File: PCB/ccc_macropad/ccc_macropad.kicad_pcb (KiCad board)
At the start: 2 copper layers, 101.5 x 44 mm, 18 parts, among them SW1 SW_Push, SW2 SW_Push, SW3 OS/Left_Right-hand_Switch, SW4 SW_Push, SW5 SW_Push, U2 XIAO-RP2040-DIP

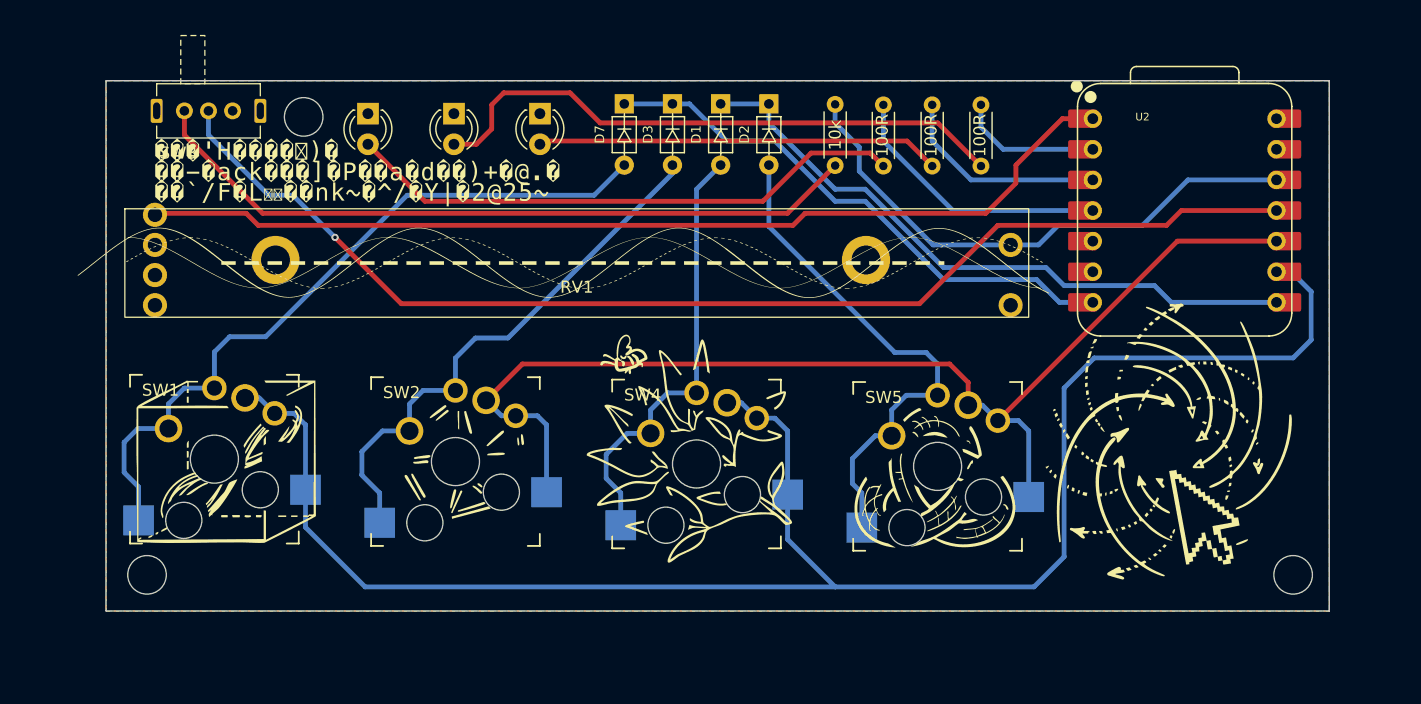
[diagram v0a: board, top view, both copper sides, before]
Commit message: feat: update schematic to rp2040_zero
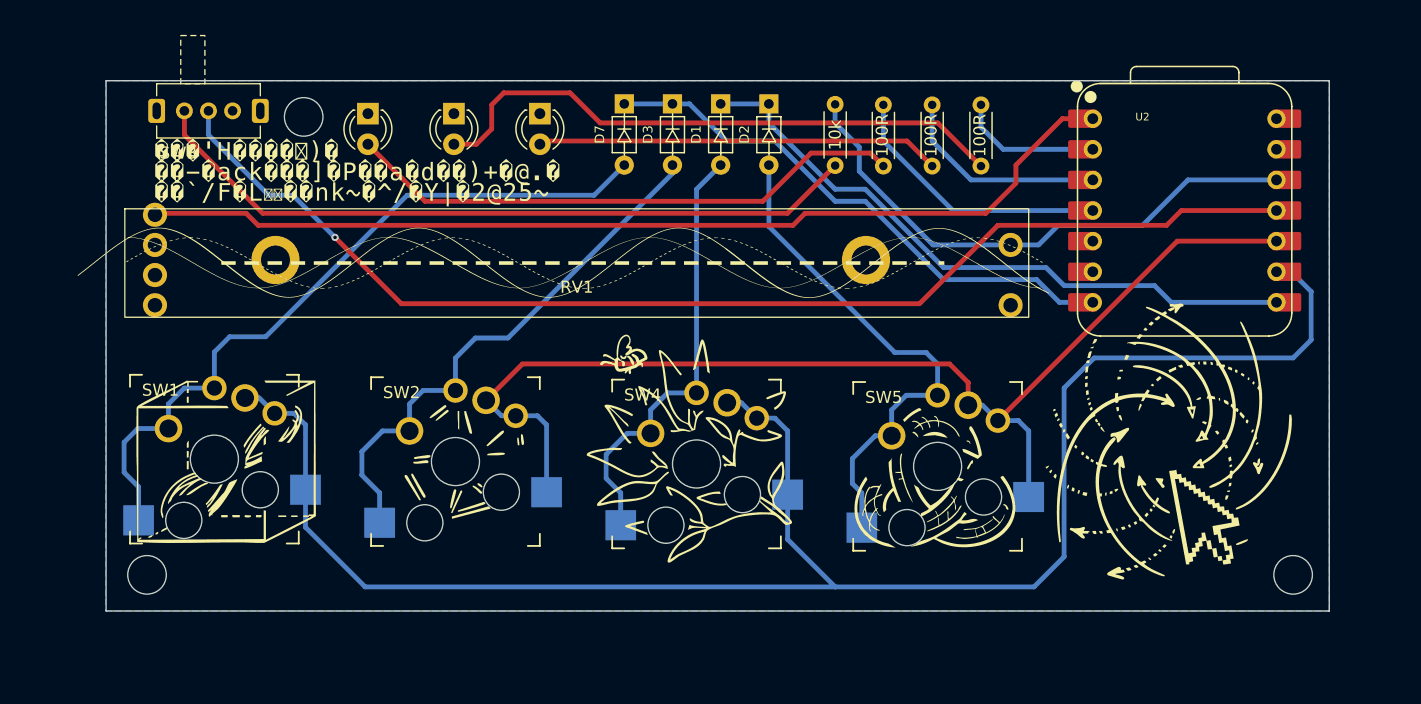
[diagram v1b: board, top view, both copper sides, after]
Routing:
- removed copper zone on F.Cu, net GND

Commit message: PCB: feat: new rp2040_zero footprint / rounded edges
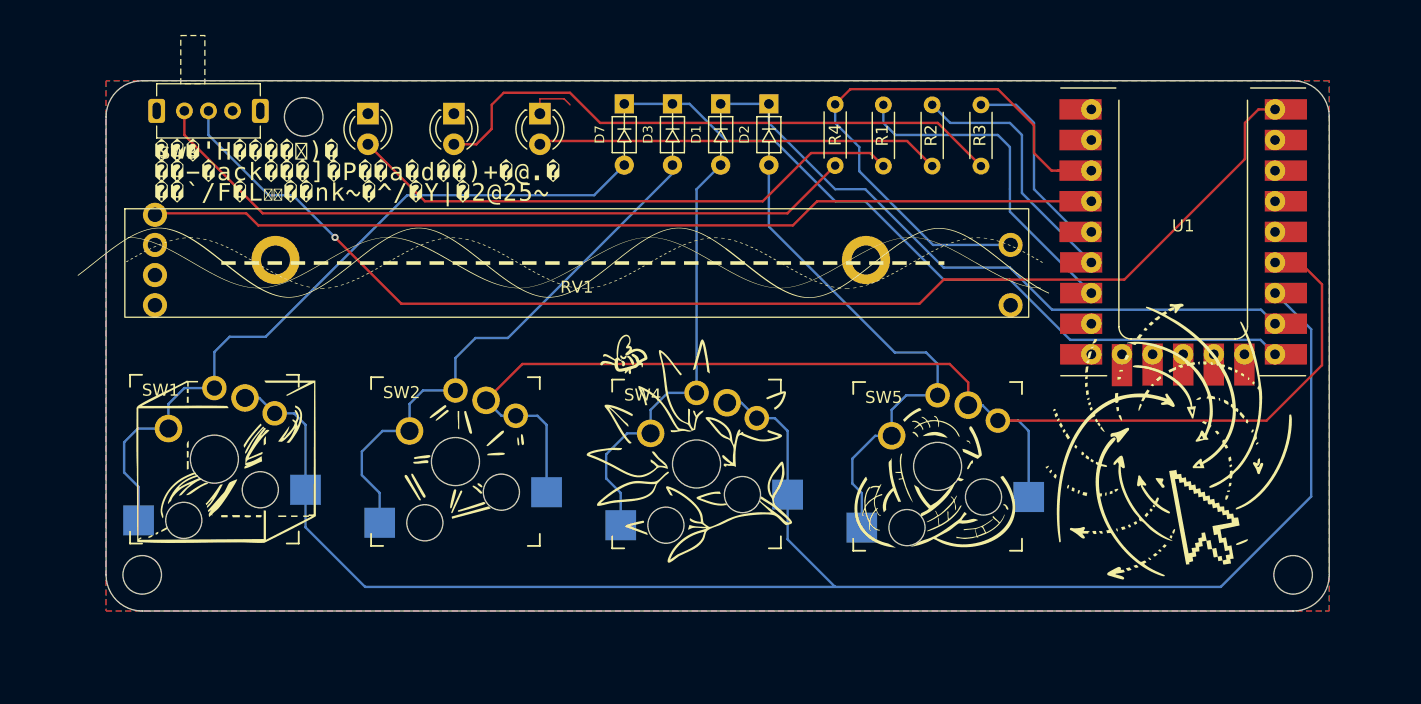
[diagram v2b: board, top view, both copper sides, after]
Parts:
- removed U2: XIAO-RP2040-DIP, XIAO Seeduino:XIAO-RP2040-DIP
- added U1: RP2040-Zero, CustomFootprints:RP2040 Zero, F.Cu at (189.7, 63.4)
- D6: renamed from D6 LED
- D8: renamed from D8 LED
- D9: renamed from D9 LED
- renumbered 100R to R1, 100R to R2, 100R to R3, 10k to R4
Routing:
- net Net-(D3-K): track 45.7 -> 62.6 mm
- net Net-(U1-GP5): track 95.9 -> 105.9 mm
- net Net-(SW3-B): track 99.6 -> 105.6 mm
- net Net-(U1-GP26): track 22.8 -> 27.7 mm
- net Net-(U1-GP28): track 11.9 -> 16.7 mm
- net Net-(U1-GP29): track 82.8 -> 78.1 mm
- net GND: track 0.00 -> 3.94 mm
- net Net-(U1-GP27): track 17.7 -> 21.5 mm
- net Net-(U1-3V3): track 44.8 -> 48.3 mm
- net Net-(U1-GP6): track 144.8 -> 141.7 mm
- net Net-(D1-K): track 53.9 -> 54.5 mm
- added copper zone on F.Cu, net GND
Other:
- outline, holes or cut-outs redrawn

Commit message: feat: cutout for MCU SMD mount
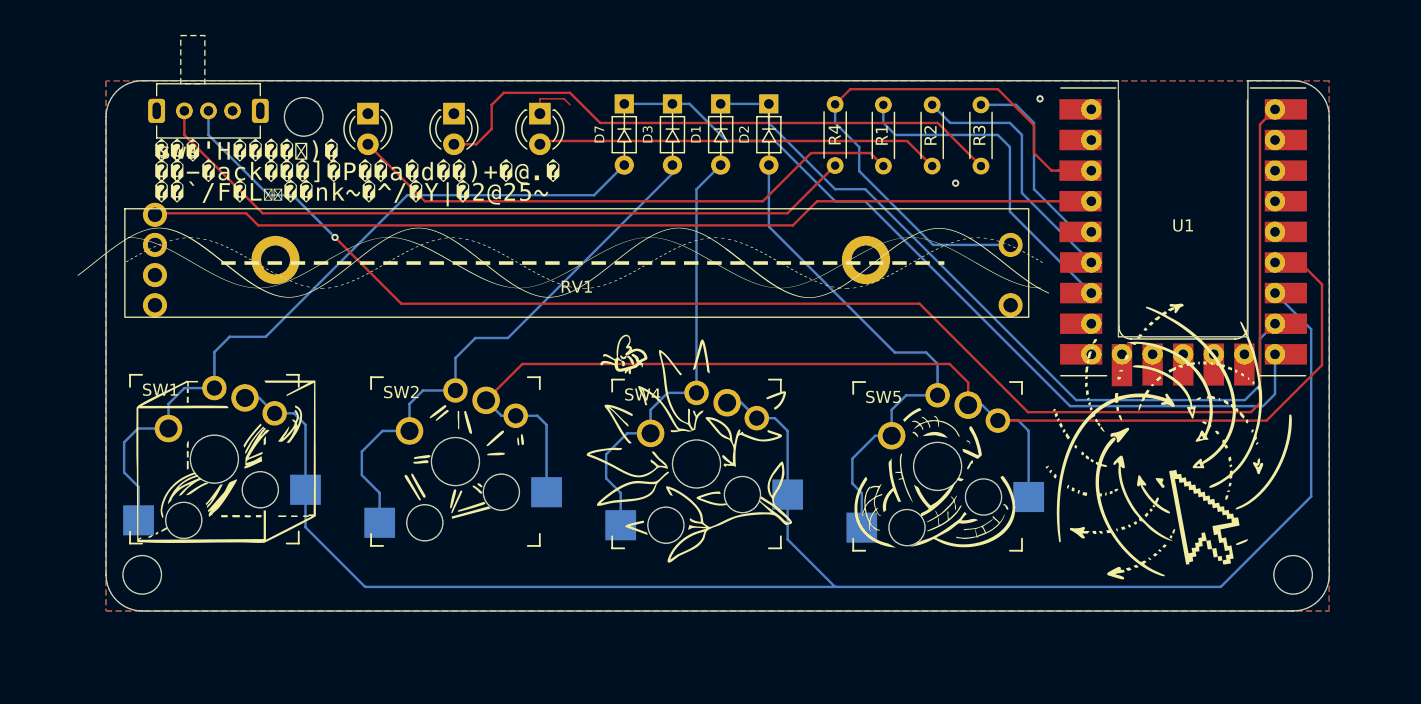
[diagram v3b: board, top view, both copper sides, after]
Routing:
- net Net-(SW3-B): track 105.6 -> 124.0 mm
- net Net-(D1-K): track 54.5 -> 62.0 mm
- net Net-(D3-K): track 62.6 -> 68.1 mm
- net GND: track 3.94 -> 4.44 mm, vias 0 -> 2
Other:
- outline, holes or cut-outs redrawn
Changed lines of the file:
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@@
+	)
+	(gr_line
+		(start 194.505 59.25)
+		(end 205.255 59.25)
+		(stroke
+			(width 0.0381)
+			(type default)
+		)
+		(layer "Edge.Cuts")
 	)
 	(gr_line
@@
 		(layer "Edge.Cuts")
 	)
+	(gr_line
+		(start 194.5 38)
+		(end 194.505 59.25)
+		(stroke
+			(width 0.0381)
+			(type default)
+		)
+		(layer "Edge.Cuts")
+	)
 	(gr_arc
 		(start 110.5 41)
@@
 		(layer "Edge.Cuts")
 	)
+	(gr_line
+		(start 205.25 59.25)
+		(end 205.25 38)
+		(stroke
+			(width 0.0381)
+			(type default)
+		)
+		(layer "Edge.Cuts")
+	)
+	(gr_line
+		(start 209 38)
+		(end 205.25 38)
+		(stroke
+			(width 0.0381)
+			(type default)
+		)
+		(layer "Edge.Cuts")
+	)
 	(gr_circle
 		(center 113.5 79)
@@
 	(gr_line
 		(start 113.5 38)
-		(end 209 38)
+		(end 194.5 38)
 		(stroke
 			(width 0.0381)
@@
 	)
 	(segment
+		(start 165.5 41.5)
+		(end 171 47)
+		(width 0.2)
+		(layer "B.Cu")
+		(net 2)
+	)
+	(segment
+		(start 191 64.5)
+		(end 205 64.5)
+		(width 0.2)
+		(layer "B.Cu")
+		(net 2)
+	)
+	(segment
 		(start 171 47)
-		(end 165.5 41.5)
+		(end 173.5 47)
+		(width 0.2)
+		(layer "B.Cu")
+		(net 2)
+	)
+	(segment
+		(start 205 64.5)
+		(end 206.25 63.25)
 		(width 0.2)
 		(layer "B.Cu")
@@
 	)
 	(segment
-		(start 189 57)
-		(end 206.34 57)
+		(start 165.5 39.92)
+		(end 165.5 41.5)
 		(width 0.2)
 		(layer "B.Cu")
@@
 	)
 	(segment
-		(start 165.5 41.5)
-		(end 165.5 39.92)
+		(start 206.25 63.25)
+		(end 206.25 59.41)
 		(width 0.2)
 		(layer "B.Cu")
@@
 	)
 	(segment
-		(start 185.5 53.5)
-		(end 189 57)
+		(start 173.5 47)
+		(end 191 64.5)
 		(width 0.2)
 		(layer "B.Cu")
@@
 	)
 	(segment
-		(start 180 53.5)
-		(end 173.5 47)
-		(width 0.2)
-		(layer "B.Cu")
-		(net 2)
-	)
-	(segment
-		(start 173.5 47)
-		(end 171 47)
-		(width 0.2)
-		(layer "B.Cu")
-		(net 2)
-	)
-	(segment
-		(start 206.34 57)
+		(start 206.25 59.41)
 		(end 207.5 58.16)
-		(width 0.2)
-		(layer "B.Cu")
-		(net 2)
-	)
-	(segment
-		(start 180 53.5)
-		(end 185.5 53.5)
 		(width 0.2)
 		(layer "B.Cu")
@@
 	)
 	(segment
-		(start 206.3 59.5)
-		(end 207.5 60.7)
+		(start 158.92 39.92)
+		(end 162 43)
+		(width 0.2)
+		(layer "B.Cu")
+		(net 4)
+	)
+	(segment
+		(start 206.5 65)
+		(end 207.5 64)
 		(width 0.2)
 		(layer "B.Cu")
@@
 	)
 	(segment
+		(start 162 43)
+		(end 166 43)
+		(width 0.2)
+		(layer "B.Cu")
+		(net 4)
+	)
+	(segment
 		(start 166 43)
 		(end 171 48)
@@
 	)
 	(segment
-		(start 185.5 54.5)
-		(end 190.5 59.5)
-		(width 0.2)
-		(layer "B.Cu")
-		(net 4)
-	)
-	(segment
-		(start 158.92 39.92)
-		(end 162 43)
-		(width 0.2)
-		(layer "B.Cu")
-		(net 4)
-	)
-	(segment
 		(start 173.5 48)
-		(end 180 54.5)
-		(width 0.2)
-		(layer "B.Cu")
-		(net 4)
-	)
-	(segment
-		(start 162 43)
-		(end 166 43)
+		(end 190.5 65)
 		(width 0.2)
 		(layer "B.Cu")
@@
 	)
 	(segment
-		(start 180 54.5)
-		(end 185.5 54.5)
+		(start 207.5 64)
+		(end 207.5 60.7)
 		(width 0.2)
 		(layer "B.Cu")
@@
 	)
 	(segment
-		(start 190.5 59.5)
-		(end 206.3 59.5)
+		(start 190.5 65)
+		(end 206.5 65)
 		(width 0.2)
 		(layer "B.Cu")
@@
 		(net 8)
 	)
+	(via
+		(at 188 39.5)
+		(size 0.6)
+		(drill 0.3)
+		(layers "F.Cu" "B.Cu")
+		(free yes)
+		(net 8)
+	)
+	(via
+		(at 181 46.5)
+		(size 0.6)
+		(drill 0.3)
+		(layers "F.Cu" "B.Cu")
+		(free yes)
+		(net 8)
+	)
+	(segment
+		(start 188 39.75)
+		(end 188 39.5)
+		(width 0.127)
+		(layer "B.Cu")
+		(net 8)
+	)
+	(segment
+		(start 181 46.25)
+		(end 181 46.5)
+		(width 0.127)
+		(layer "B.Cu")
+		(net 8)
+	)
 	(segment
 		(start 146.5 43.27)
@@
 	)
 	(segment
-		(start 205 44.5)
-		(end 205 41.5)
+		(start 187 65.5)
+		(end 205.5 65.5)
+		(width 0.2)
+		(layer "F.Cu")
+		(net 12)
+	)
+	(segment
+		(start 206.25 64.75)
+		(end 206.25 41.63)
 		(width 0.2)
 		(layer "F.Cu")
@@
 	)
 	(segment
-		(start 195 54.5)
-		(end 205 44.5)
-		(width 0.2)
-		(layer "F.Cu")
-		(net 12)
-	)
-	(segment
-		(start 205 41.5)
-		(end 206.12 40.38)
-		(width 0.2)
-		(layer "F.Cu")
-		(net 12)
-	)
-	(segment
 		(start 129.5 51)
 		(end 135 56.5)
@@
 	)
 	(segment
-		(start 206.12 40.38)
-		(end 208.4 40.38)
+		(start 206.25 41.63)
+		(end 207.5 40.38)
 		(width 0.2)
 		(layer "F.Cu")
@@
 	)
 	(segment
-		(start 180 54.5)
-		(end 195 54.5)
+		(start 178 56.5)
+		(end 187 65.5)
 		(width 0.2)
 		(layer "F.Cu")
@@
 	)
 	(segment
-		(start 178 56.5)
-		(end 180 54.5)
-		(width 0.2)
-		(layer "F.Cu")
+		(start 205.5 65.5)
+		(end 206.25 64.75)
+		(width 0.2)
+		(layer "F.Cu")

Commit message: added art to back: silkscreen and exposed copper
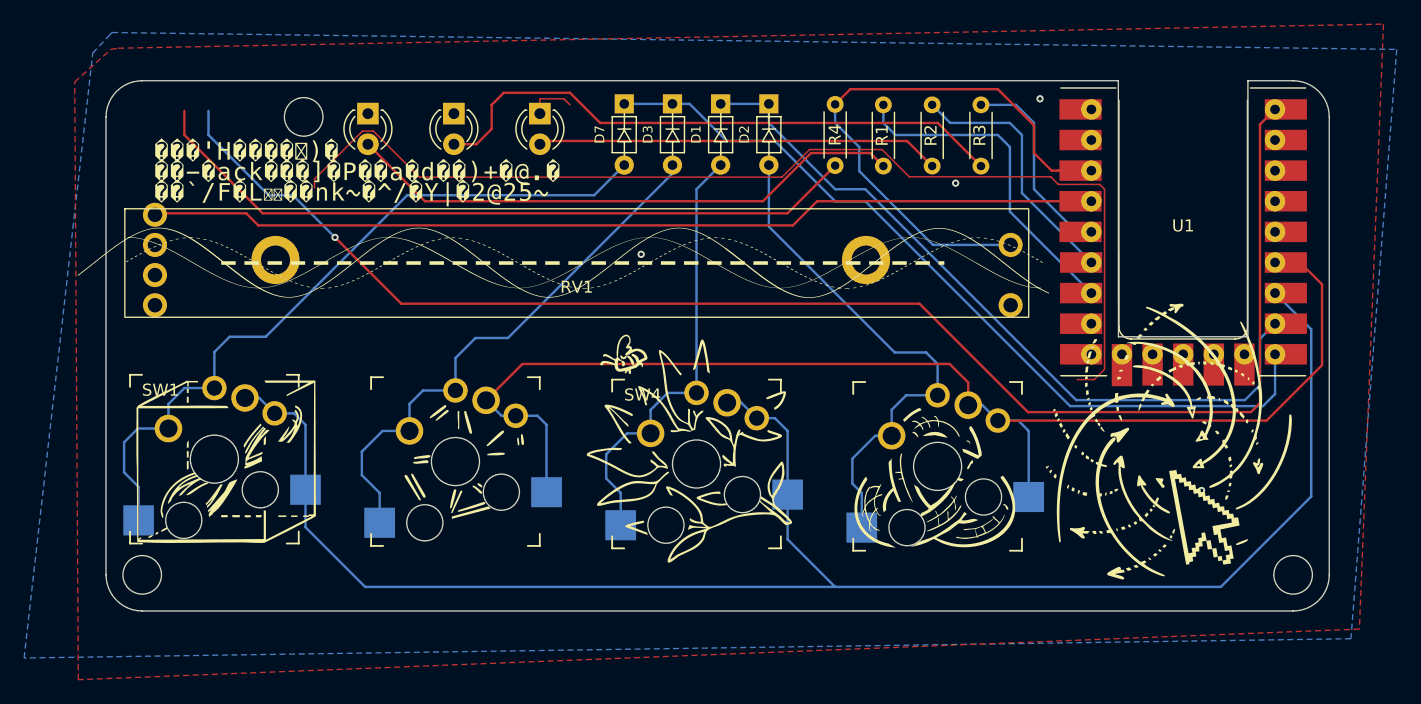
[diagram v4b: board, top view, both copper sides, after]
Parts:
- removed SW3: OS/Left_Right-hand_Switch, CustomFootprints:SPDT_3pin_2_pos_1P2T_tht_2.54mm_switch_sk12d07
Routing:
- net (no net): track 0.00 -> 89.4 mm
- net GND: track 4.44 -> 4.72 mm, vias 2 -> 4
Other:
- board text added: "${REFERENCE}"
